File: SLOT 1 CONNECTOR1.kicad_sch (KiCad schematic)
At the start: 18 parts, among them J33 Slot1

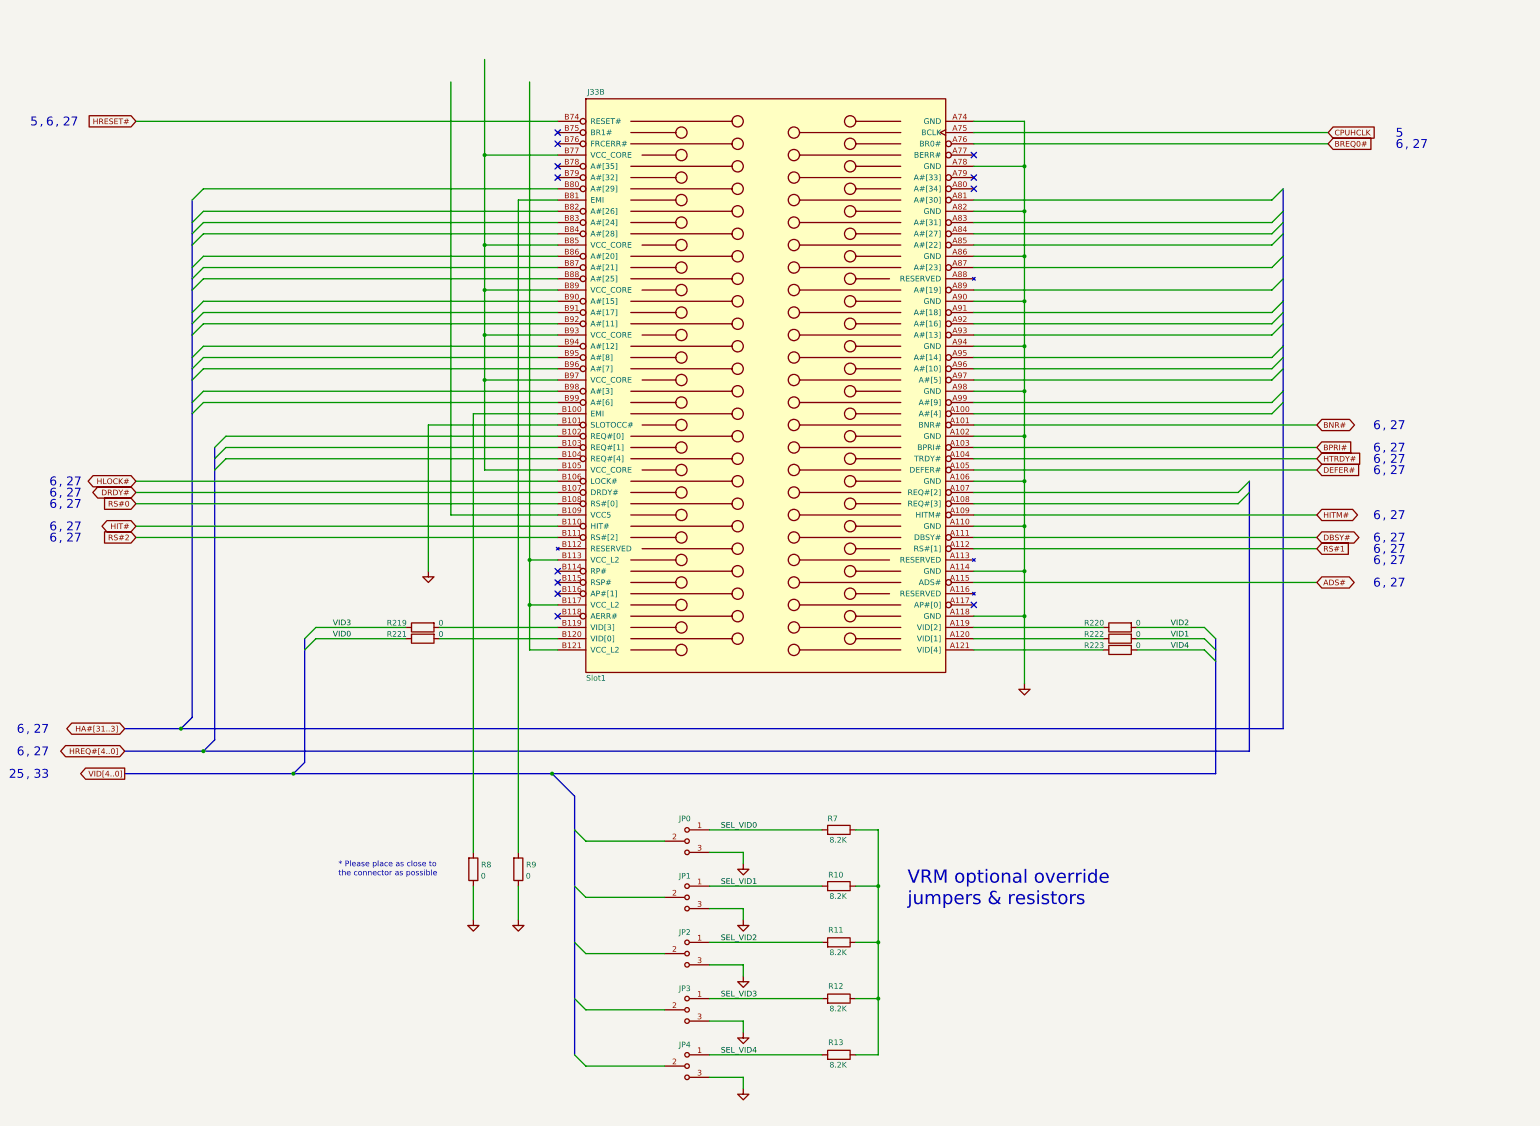
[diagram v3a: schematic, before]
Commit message: page 18 ISA, small fixes
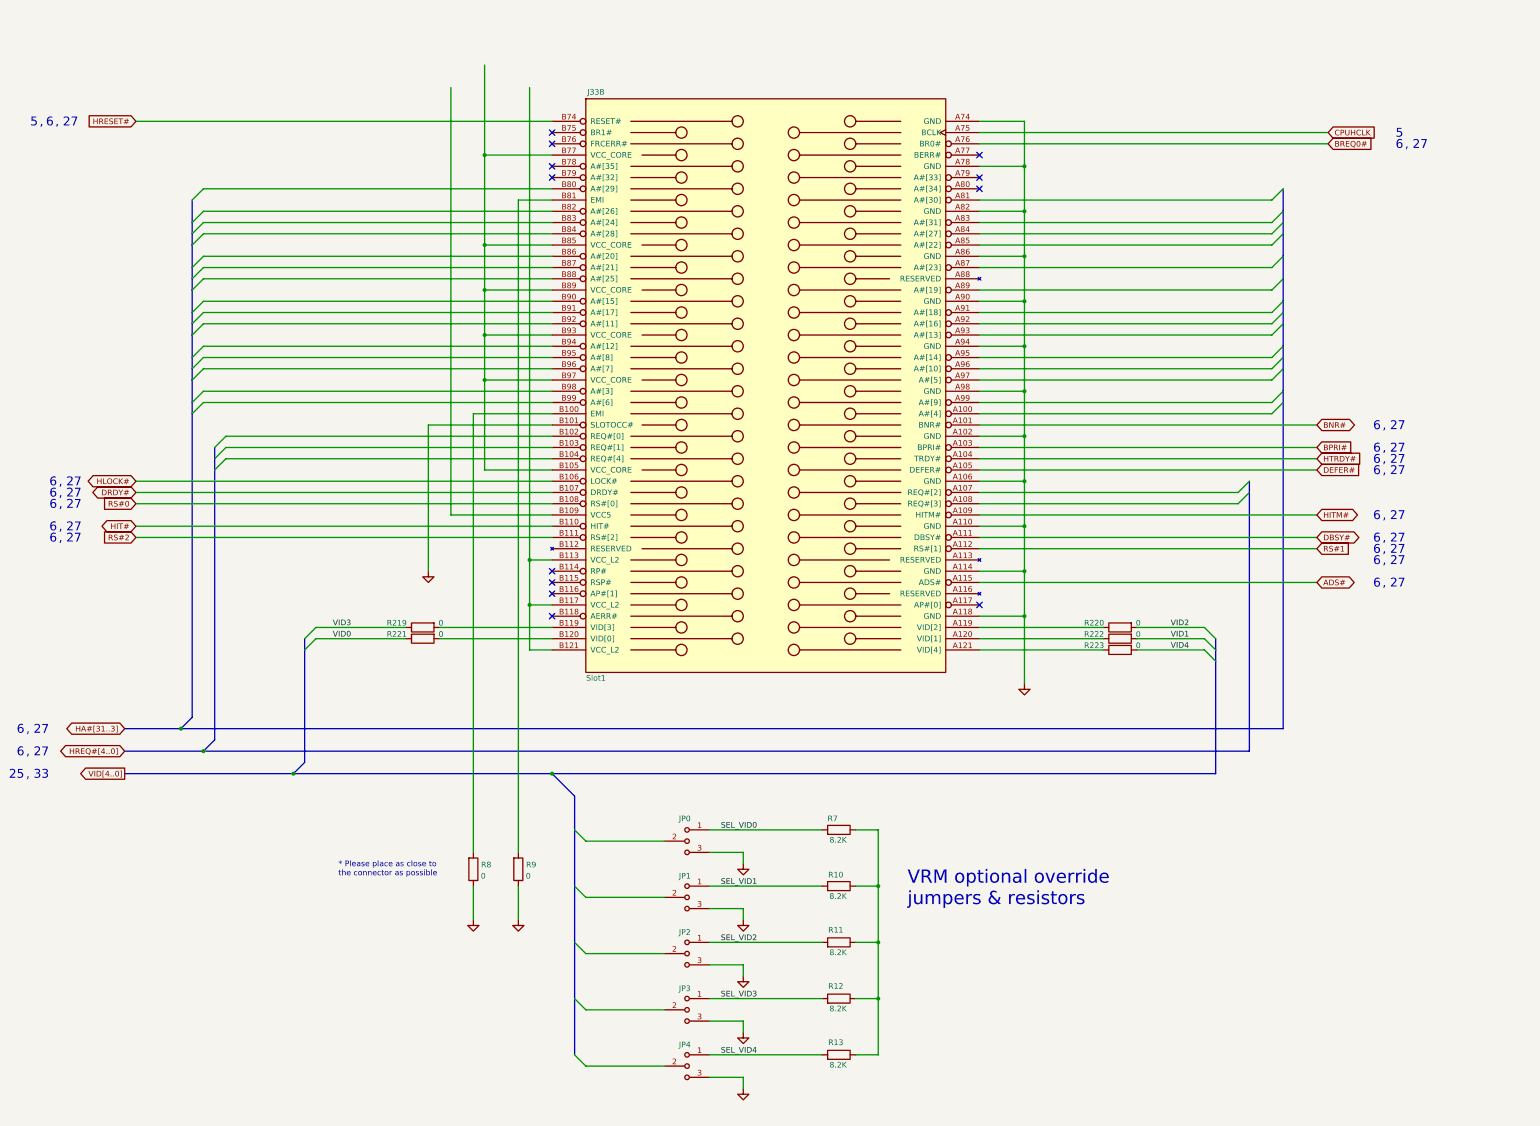
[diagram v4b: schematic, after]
